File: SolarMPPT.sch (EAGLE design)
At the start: 42 parts, among them J1 CORTEX_DEBUG_SMD, U1 STM32F091CCT6, U3 LTC1155, U4 LM22674MRX-5.0, U5 3.3V

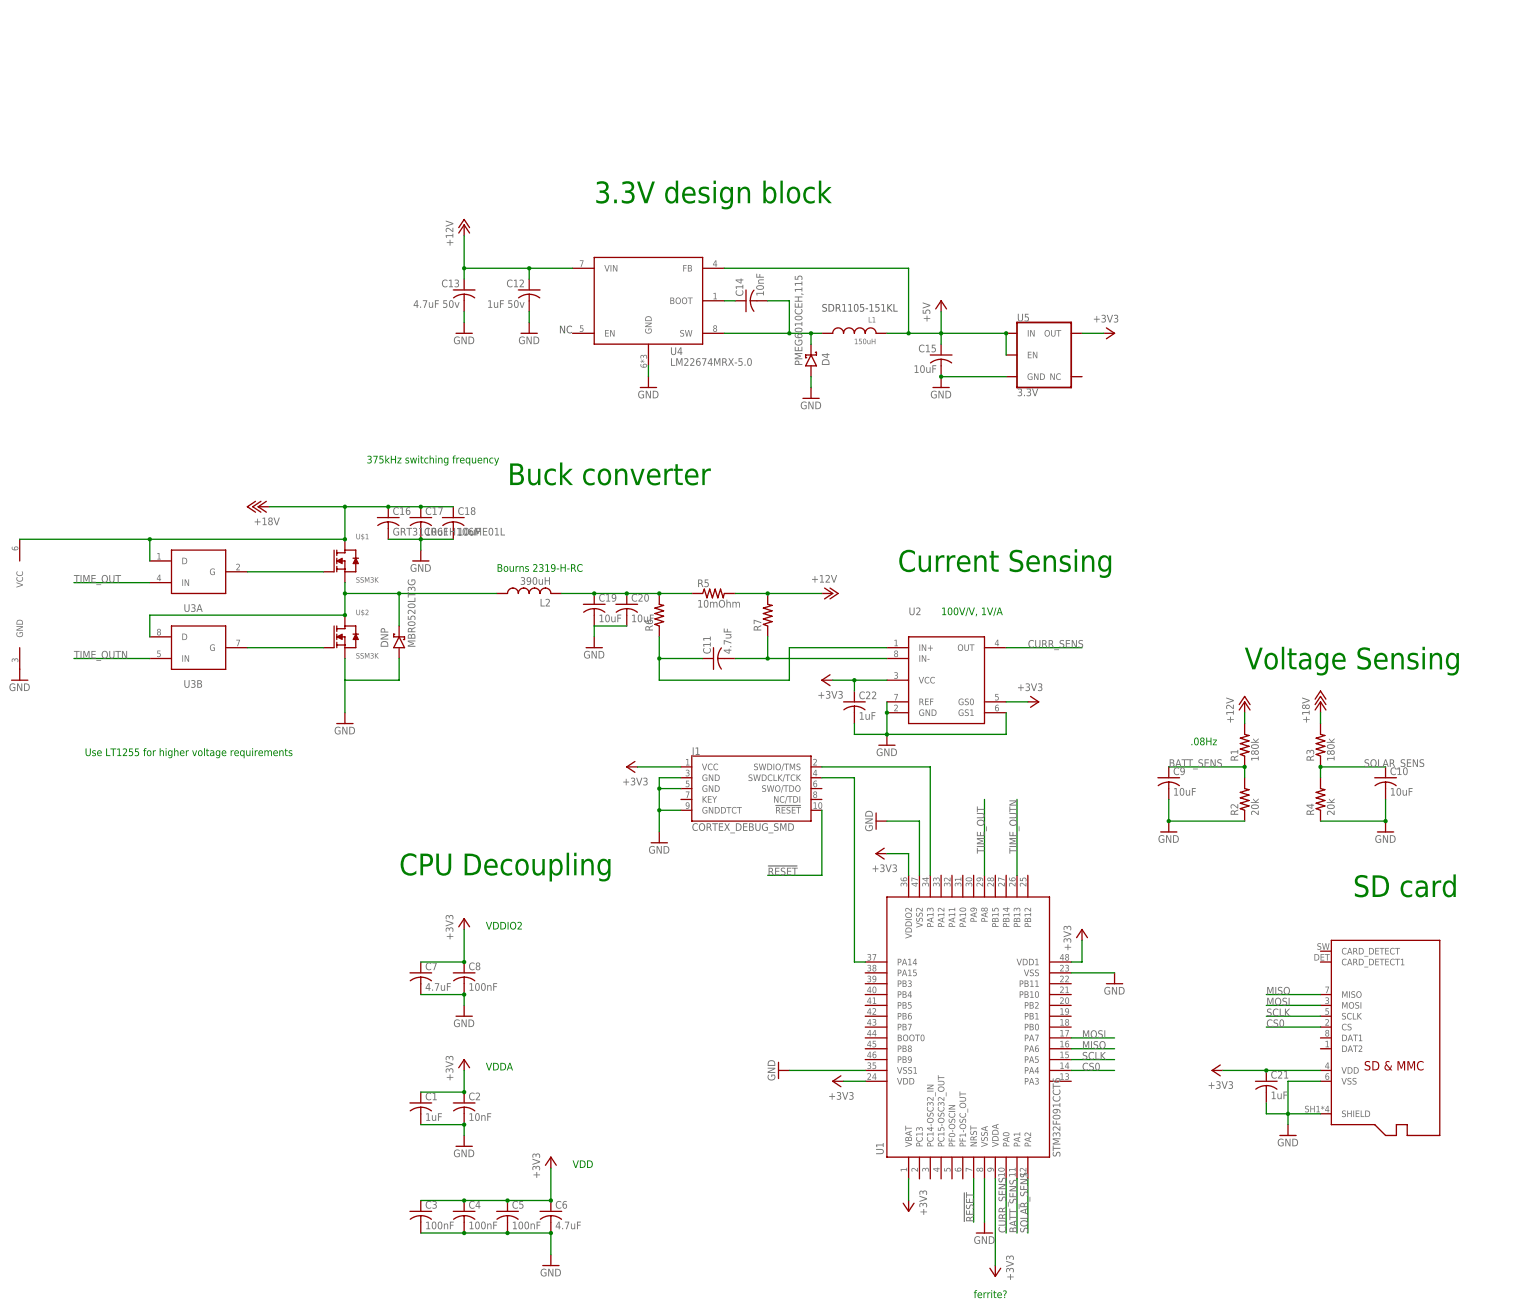
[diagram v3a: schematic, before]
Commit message: created brd file and sorted into categories
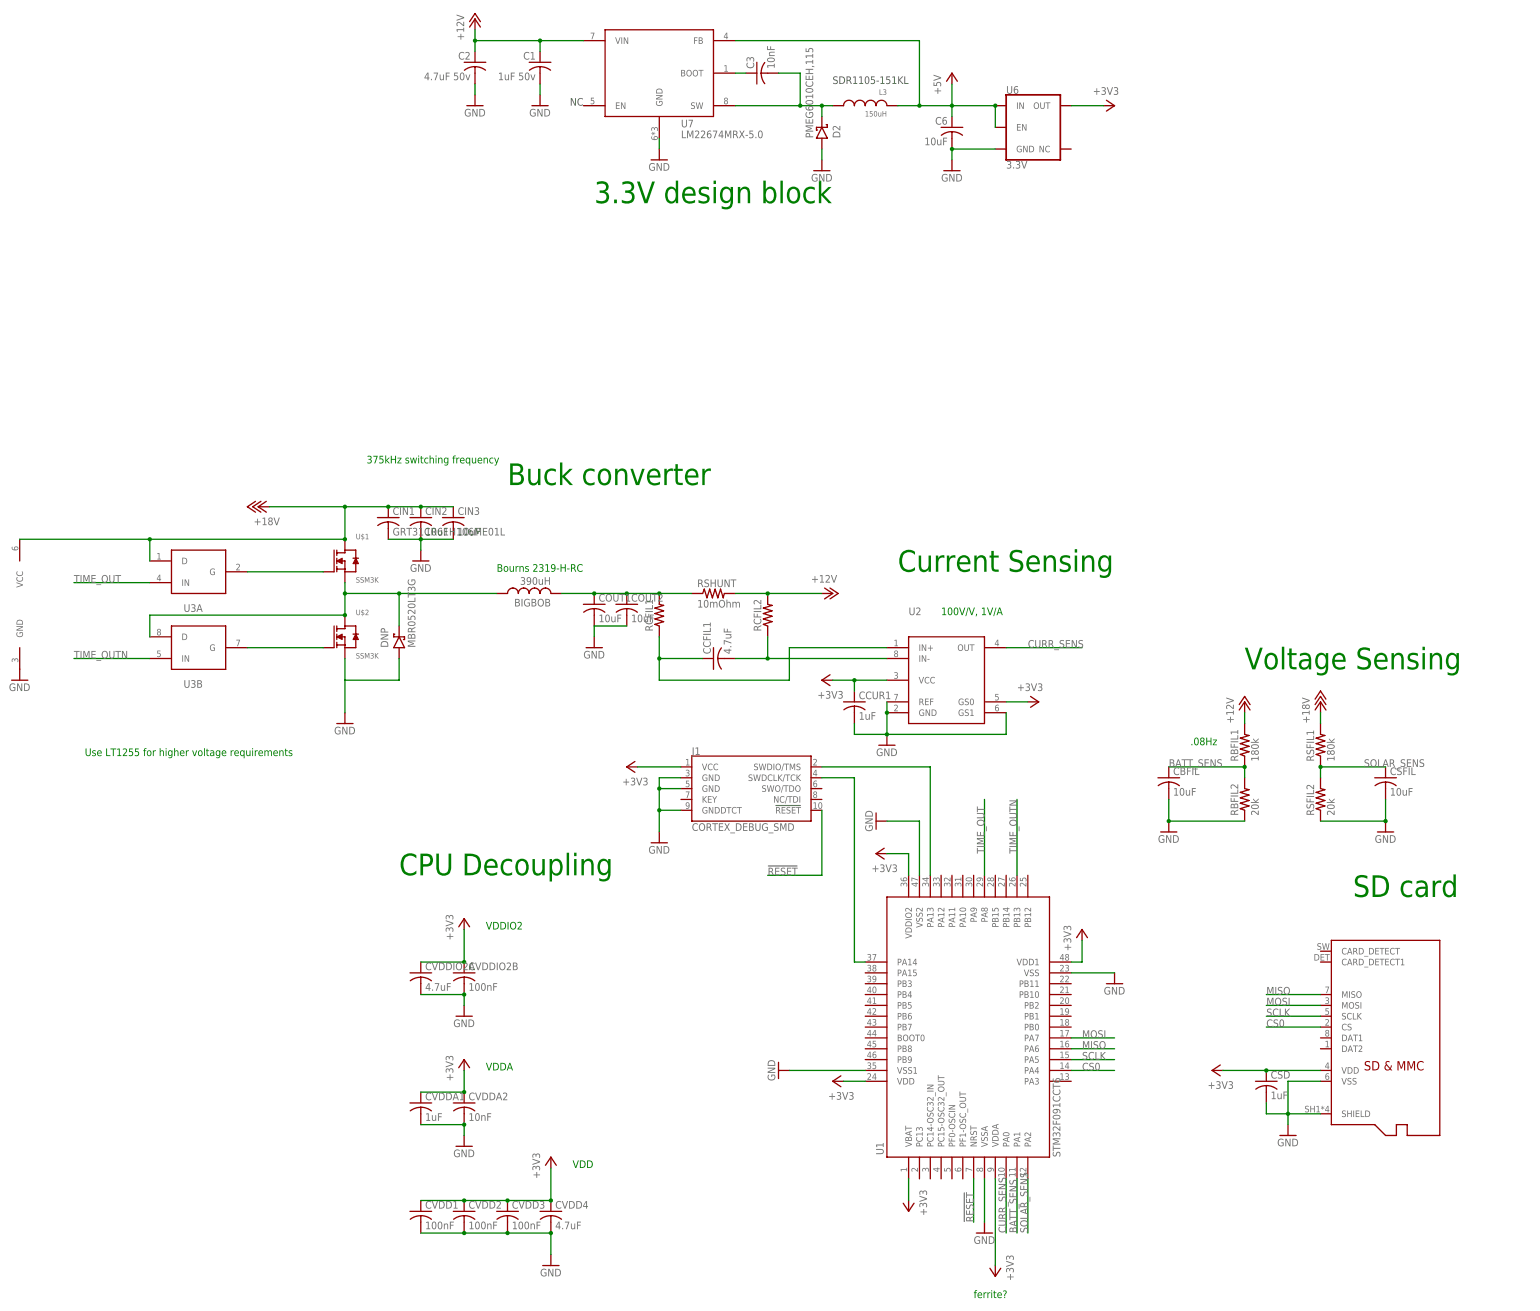
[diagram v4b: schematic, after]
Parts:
- removed C12: 1uF 50v, rcl:C-USC0805
- removed C13: 4.7uF 50v, rcl:C-USC1206
- removed C14: 10nF, rcl:C-USC0805
- removed C15: 10uF, rcl:C-USC0805
- removed D4: PMEG6010CEH,115, FormE:PMEG6010CEH,115
- removed L1: 150uH, FormE:SDR1105
- removed U4: LM22674MRX-5.0, FormE:LM22674
- removed U5: 3.3V, SparkFun-IC-Power:V_REG_AP2112K-3.3V
- added CVDD1: 100nF, rcl:C-USC0805
- added CVDD4: 4.7uF, rcl:C-USC0805
- added CVDDA1: 1uF, rcl:C-USC0805
- added CVDDA2: 10nF, rcl:C-USC0805
- added D2: PMEG6010CEH,115, FormE:PMEG6010CEH,115
- added L3: 150uH, FormE:SDR1105
- added U6: 3.3V, SparkFun-IC-Power:V_REG_AP2112K-3.3V
- added U7: LM22674MRX-5.0, FormE:LM22674
- C1: value 1uF -> 1uF 50v; PARTNO (none) -> UMK212BJ105KG-T
- C2: value 10nF -> 4.7uF 50v; device rcl:C-USC0805 -> rcl:C-USC1206; PARTNO (none) -> GRM31CR71H475KA12L
- C3: value 100nF -> 10nF; PARTNO (none) -> GRM216R71H103KA01D
- C6: value 4.7uF -> 10uF; PARTNO (none) -> GRM21BR61E106KA73L
- renumbered C10 to CSFIL, C11 to CCFIL1, C16 to CIN1, C17 to CIN2, C18 to CIN3, C19 to COUT1, C20 to COUT2, C21 to CSD, C22 to CCUR1, C4 to CVDD2, C5 to CVDD3, C7 to CVDDIO2A, C8 to CVDDIO2B, C9 to CBFIL, L2 to BIGBOB, R1 to RBFIL1, R2 to RBFIL2, R3 to RSFIL1, R4 to RSFIL2, R5 to RSHUNT, R6 to RCFIL1, R7 to RCFIL2
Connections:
- removed net BOOT_5V: C14.1, U4.BOOT
- removed net SW_5V: C14.2, D4.K, L1.P$2, U4.SW
- new net BOOT_5V2: C3.1, U7.BOOT
- new net SW_5V2: C3.2, D2.K, L3.P$2, U7.SW
- net +12V: now also C1.1, C2.1, U7.VIN; no longer C12.1, C13.1, U4.VIN
- net +3V3: now also CVDD1.1, CVDD4.1, CVDDA1.1, CVDDA2.1, U6.OUT; no longer C1.1, C2.1, C3.1, C6.1, U5.OUT
- net +5V: now also C6.1, L3.P$1, U6.EN, U6.IN, U7.FB; no longer C15.1, L1.P$1, U4.FB, U5.EN, U5.IN
- net GND: now also CVDD1.2, CVDD4.2, CVDDA1.2, CVDDA2.2, D2.A, U6.GND, U7.GND; no longer C12.2, C13.2, C15.2, C3.2, D4.A, U4.GND, U5.GND
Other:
- moved on the sheet: C1, C2, C3, C6

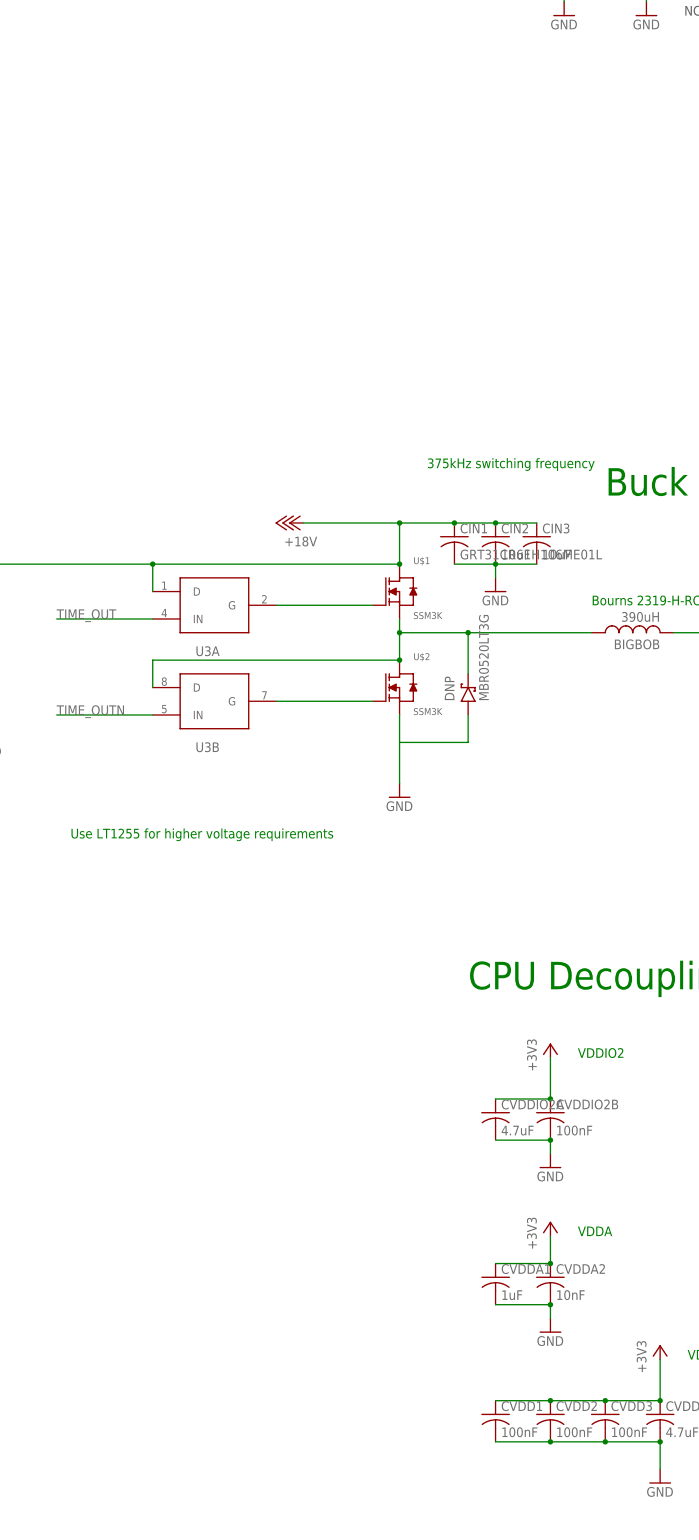
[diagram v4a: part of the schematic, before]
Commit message: Did power routing and added terminals
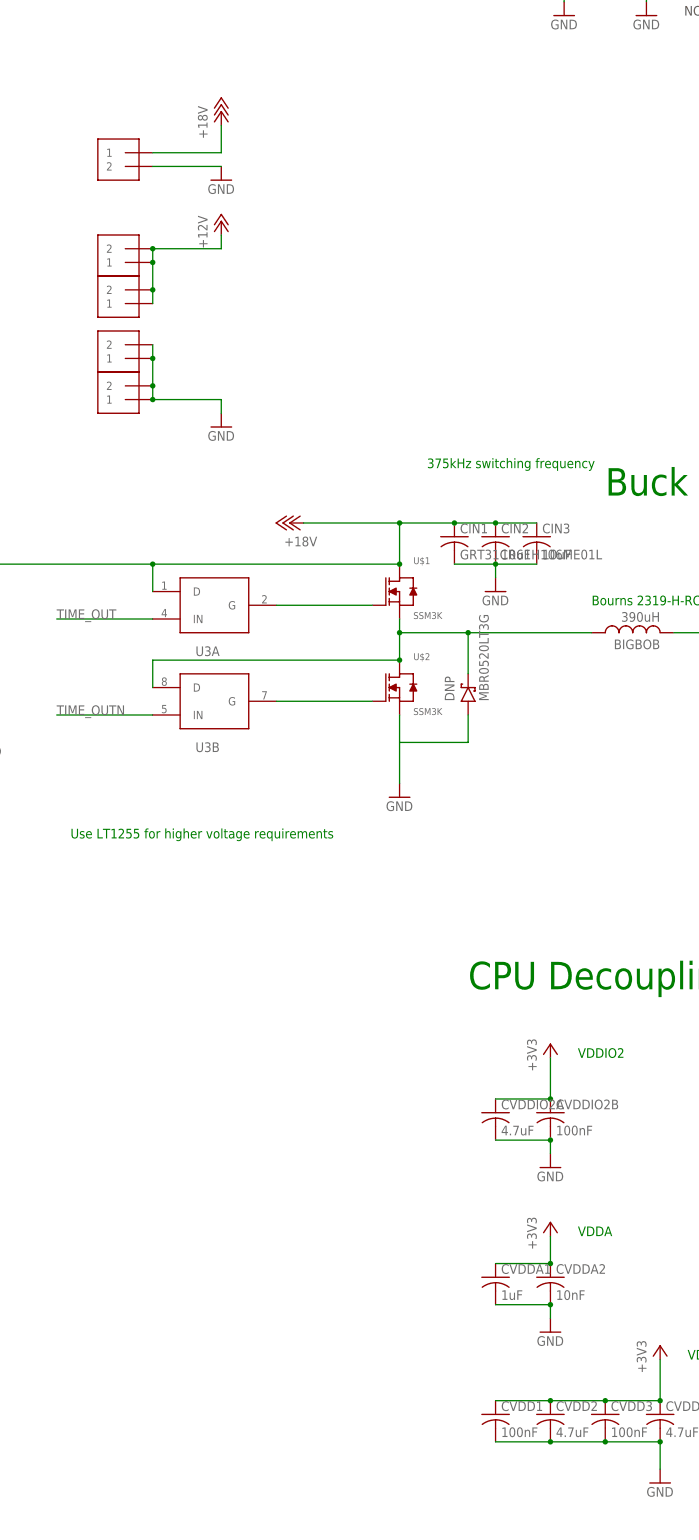
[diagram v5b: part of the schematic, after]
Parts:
- added J2, J3, J4, J5, J6: 1X2-3.5MM, adafruit:1X2-3.5MM
- CVDD2: value 100nF -> 4.7uF
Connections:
- net +12V: now also J2.1, J2.2, J3.1, J3.2
- net +18V: now also J6.1
- net GND: now also J4.1, J4.2, J5.1, J5.2, J6.2
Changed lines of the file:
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@@
 <part name="CVDDA2" library="rcl" library_urn="urn:adsk.eagle:library:334" deviceset="C-US" device="C0805" package3d_urn="urn:adsk.eagle:package:23617/2" value="10nF"/>
 <part name="CVDD1" library="rcl" library_urn="urn:adsk.eagle:library:334" deviceset="C-US" device="C0805" package3d_urn="urn:adsk.eagle:package:23617/2" value="100nF"/>
-<part name="CVDD2" library="rcl" library_urn="urn:adsk.eagle:library:334" deviceset="C-US" device="C0805" package3d_urn="urn:adsk.eagle:package:23617/2" value="100nF"/>
+<part name="CVDD2" library="rcl" library_urn="urn:adsk.eagle:library:334" deviceset="C-US" device="C0805" package3d_urn="urn:adsk.eagle:package:23617/2" value="4.7uF"/>
 <part name="CVDD3" library="rcl" library_urn="urn:adsk.eagle:library:334" deviceset="C-US" device="C0805" package3d_urn="urn:adsk.eagle:package:23617/2" value="100nF"/>
 <part name="CVDD4" library="rcl" library_urn="urn:adsk.eagle:library:334" deviceset="C-US" device="C0805" package3d_urn="urn:adsk.eagle:package:23617/2" value="4.7uF"/>
@@
 <part name="U6" library="SparkFun-IC-Power" library_urn="urn:adsk.eagle:library:526" deviceset="V_REG_AP2112" device="K-3.3V" package3d_urn="urn:adsk.eagle:package:39060/1" value="3.3V"/>
 <part name="+3V14" library="supply1" library_urn="urn:adsk.eagle:library:371" deviceset="+3V3" device=""/>
+<part name="J2" library="adafruit" library_urn="urn:adsk.eagle:library:420" deviceset="1X2" device="-3.5MM" package3d_urn="urn:adsk.eagle:package:6240635/1"/>
+<part name="J3" library="adafruit" library_urn="urn:adsk.eagle:library:420" deviceset="1X2" device="-3.5MM" package3d_urn="urn:adsk.eagle:package:6240635/1"/>
+<part name="J4" library="adafruit" library_urn="urn:adsk.eagle:library:420" deviceset="1X2" device="-3.5MM" package3d_urn="urn:adsk.eagle:package:6240635/1"/>
+<part name="J5" library="adafruit" library_urn="urn:adsk.eagle:library:420" deviceset="1X2" device="-3.5MM" package3d_urn="urn:adsk.eagle:package:6240635/1"/>
+<part name="J6" library="adafruit" library_urn="urn:adsk.eagle:library:420" deviceset="1X2" device="-3.5MM" package3d_urn="urn:adsk.eagle:package:6240635/1"/>
+<part name="P+5" library="supply1" library_urn="urn:adsk.eagle:library:371" deviceset="+12V" device=""/>
+<part name="P+7" library="supply1" library_urn="urn:adsk.eagle:library:371" deviceset="+18V" device=""/>
+<part name="GND13" library="supply1" library_urn="urn:adsk.eagle:library:371" deviceset="GND" device=""/>
+<part name="GND14" library="supply1" library_urn="urn:adsk.eagle:library:371" deviceset="GND" device=""/>
 </parts>
 <sheets>
@@
 <attribute name="VALUE" x="48.26" y="284.48" size="1.778" layer="96"/>
 </instance>
+<instance part="J2" gate="G$1" x="-177.8" y="238.76" smashed="yes" rot="R180"/>
+<instance part="J3" gate="G$1" x="-177.8" y="231.14" smashed="yes" rot="R180"/>
+<instance part="J4" gate="G$1" x="-177.8" y="220.98" smashed="yes" rot="R180"/>
+<instance part="J5" gate="G$1" x="-177.8" y="213.36" smashed="yes" rot="R180"/>
+<instance part="J6" gate="G$1" x="-177.8" y="254" smashed="yes" rot="MR0"/>
+<instance part="P+5" gate="1" x="-160.02" y="243.84" smashed="yes">
+<attribute name="VALUE" x="-162.56" y="238.76" size="1.778" layer="96" rot="R90"/>
+</instance>
+<instance part="P+7" gate="1" x="-160.02" y="264.16" smashed="yes">
+<attribute name="VALUE" x="-162.56" y="259.08" size="1.778" layer="96" rot="R90"/>
+</instance>
+<instance part="GND13" gate="1" x="-160.02" y="205.74" smashed="yes">
+<attribute name="VALUE" x="-162.56" y="203.2" size="1.778" layer="96"/>
+</instance>
+<instance part="GND14" gate="1" x="-160.02" y="251.46" smashed="yes">
+<attribute name="VALUE" x="-162.56" y="248.92" size="1.778" layer="96"/>
+</instance>
 </instances>
 <busses>
@@
 <junction x="15.24" y="271.78"/>
 </segment>
+<segment>
+<pinref part="J5" gate="G$1" pin="1"/>
+<wire x1="-172.72" y1="210.82" x2="-160.02" y2="210.82" width="0.1524" layer="91"/>
+<pinref part="GND13" gate="1" pin="GND"/>
+<wire x1="-160.02" y1="210.82" x2="-160.02" y2="208.28" width="0.1524" layer="91"/>
+<pinref part="J5" gate="G$1" pin="2"/>
+<wire x1="-172.72" y1="213.36" x2="-172.72" y2="210.82" width="0.1524" layer="91"/>
+<junction x="-172.72" y="210.82"/>
+<pinref part="J4" gate="G$1" pin="1"/>
+<wire x1="-172.72" y1="218.44" x2="-172.72" y2="213.36" width="0.1524" layer="91"/>
+<junction x="-172.72" y="213.36"/>
+<pinref part="J4" gate="G$1" pin="2"/>
+<wire x1="-172.72" y1="220.98" x2="-172.72" y2="218.44" width="0.1524" layer="91"/>
+<junction x="-172.72" y="218.44"/>
+</segment>
+<segment>
+<pinref part="J6" gate="G$1" pin="2"/>
+<pinref part="GND14" gate="1" pin="GND"/>
+<wire x1="-172.72" y1="254" x2="-160.02" y2="254" width="0.1524" layer="91"/>
+</segment>
 </net>
 <net name="N$1" class="0">
@@
 <junction x="-96.52" y="297.18"/>
 <pinref part="P+6" gate="1" pin="+12V"/>
+</segment>
+<segment>
+<pinref part="J3" gate="G$1" pin="1"/>
+<pinref part="J3" gate="G$1" pin="2"/>
+<wire x1="-172.72" y1="228.6" x2="-172.72" y2="231.14" width="0.1524" layer="91"/>
+<pinref part="J2" gate="G$1" pin="1"/>
+<junction x="-172.72" y="231.14"/>
+<pinref part="J2" gate="G$1" pin="2"/>
+<wire x1="-172.72" y1="231.14" x2="-172.72" y2="236.22" width="0.1524" layer="91"/>
+<pinref part="P+5" gate="1" pin="+12V"/>
+<wire x1="-172.72" y1="238.76" x2="-160.02" y2="238.76" width="0.1524" layer="91"/>
+<wire x1="-160.02" y1="238.76" x2="-160.02" y2="241.3" width="0.1524" layer="91"/>
+<junction x="-172.72" y="238.76"/>
+<wire x1="-172.72" y1="236.22" x2="-172.72" y2="238.76" width="0.1524" layer="91"/>
+<junction x="-172.72" y="236.22"/>
 </segment>
 </net>
@@
 <junction x="-109.22" y="187.96"/>
 </segment>
-</net>
+<segment>
+<pinref part="J6" gate="G$1" pin="1"/>
+<pinref part="P+7" gate="1" pin="+18V"/>
+<wire x1="-172.72" y1="256.54" x2="-160.02" y2="256.54" width="0.1524" layer="91"/>
+<wire x1="-160.02" y1="256.54" x2="-160.02" y2="261.62" width="0.1524" layer="91"/>
+</segment>
+</net>
